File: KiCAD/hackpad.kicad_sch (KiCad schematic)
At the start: 5 parts, among them SW1 SW_Push, SW2 SW_Push, SW3 SW_Push, U1 XIAO-SAMD21-SMD

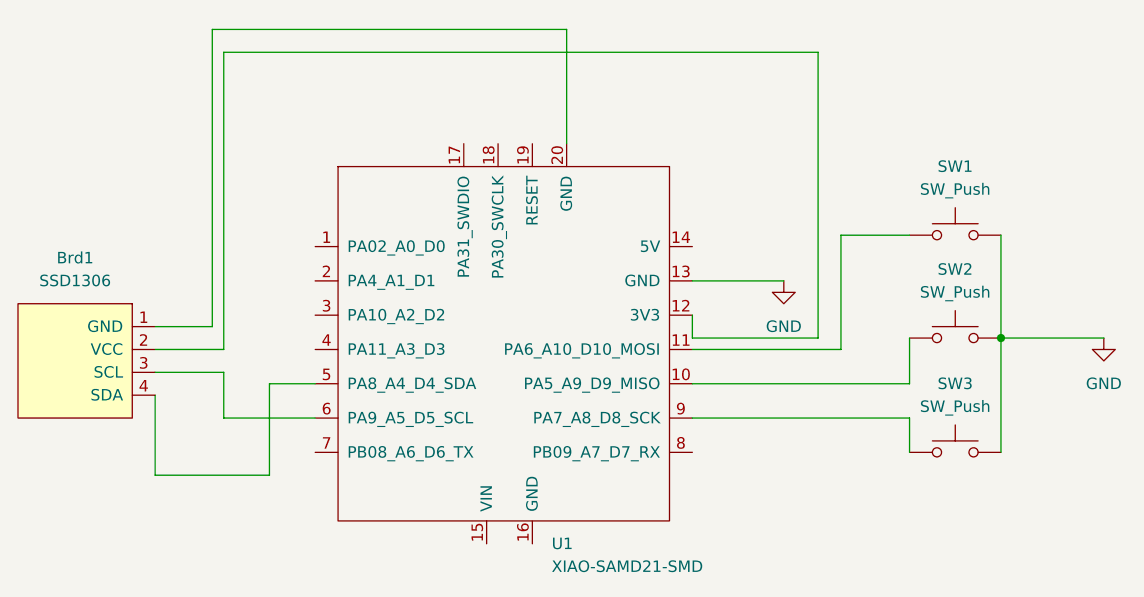
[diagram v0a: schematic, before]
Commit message: Updated the KiCad files to include the screen
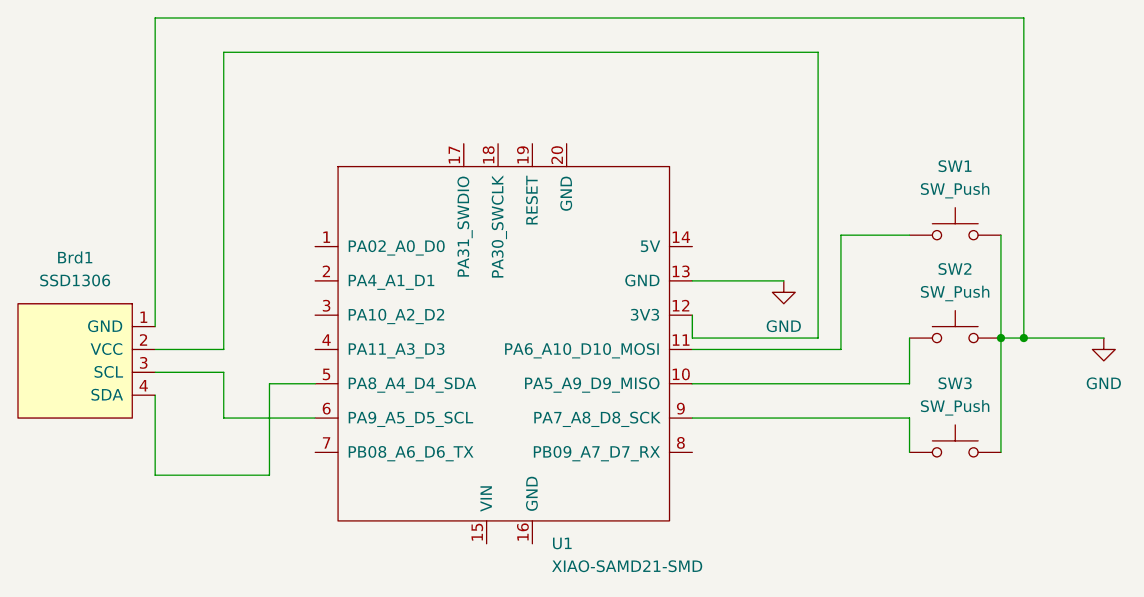
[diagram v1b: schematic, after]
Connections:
- net GND: now also Brd1.1 (GND)
- net at U1.20 (GND): no longer Brd1.1 (GND)
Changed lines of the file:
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@@
 		(color 0 0 0 0)
 	)
+	(junction
+		(at 203.2 95.25)
+		(diameter 0)
+		(color 0 0 0 0)
+	)
 	(wire
 		(pts
@@
 	(wire
 		(pts
-			(xy 200.66 95.25) (xy 212.09 95.25)
+			(xy 106.68 59.69) (xy 203.2 59.69)
+		)
+		(stroke
+			(width 0)
+			(type default)
+		)
+	)
+	(wire
+		(pts
+			(xy 200.66 95.25) (xy 203.2 95.25)
 		)
 		(stroke
@@
 	(wire
 		(pts
-			(xy 113.03 93.98) (xy 106.68 93.98)
-		)
-		(stroke
-			(width 0)
-			(type default)
-		)
-	)
-	(wire
-		(pts
 			(xy 166.37 100.33) (xy 190.5 100.33)
 		)
@@
 	(wire
 		(pts
-			(xy 113.03 60.96) (xy 113.03 93.98)
+			(xy 203.2 95.25) (xy 212.09 95.25)
 		)
 		(stroke
@@
 	(wire
 		(pts
-			(xy 152.4 60.96) (xy 113.03 60.96)
-		)
-		(stroke
-			(width 0)
-			(type default)
-		)
-	)
-	(wire
-		(pts
-			(xy 152.4 73.66) (xy 152.4 60.96)
-		)
-		(stroke
-			(width 0)
-			(type default)
-		)
-	)
-	(wire
-		(pts
 			(xy 106.68 99.06) (xy 114.3 99.06)
 		)
@@
 	(wire
 		(pts
+			(xy 106.68 93.98) (xy 106.68 59.69)
+		)
+		(stroke
+			(width 0)
+			(type default)
+		)
+	)
+	(wire
+		(pts
 			(xy 119.38 110.49) (xy 106.68 110.49)
 		)
@@
 		)
 		(stroke
+			(width 0)
+			(type default)
+		)
+	)
+	(wire
+		(pts
+			(xy 203.2 59.69) (xy 203.2 95.25)
+		)
+		(stroke
